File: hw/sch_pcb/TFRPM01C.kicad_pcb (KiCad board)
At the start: 2 copper layers, 37.5 x 19 mm, 22 parts, among them J1 HEADER_1x03, J2 SM04B-GHS-TB, J3 SM04B-GHS-TB, M2 M3, U1 PCF8583, U2 74HC1G14GW, U3 MIC5504-3.3YM5

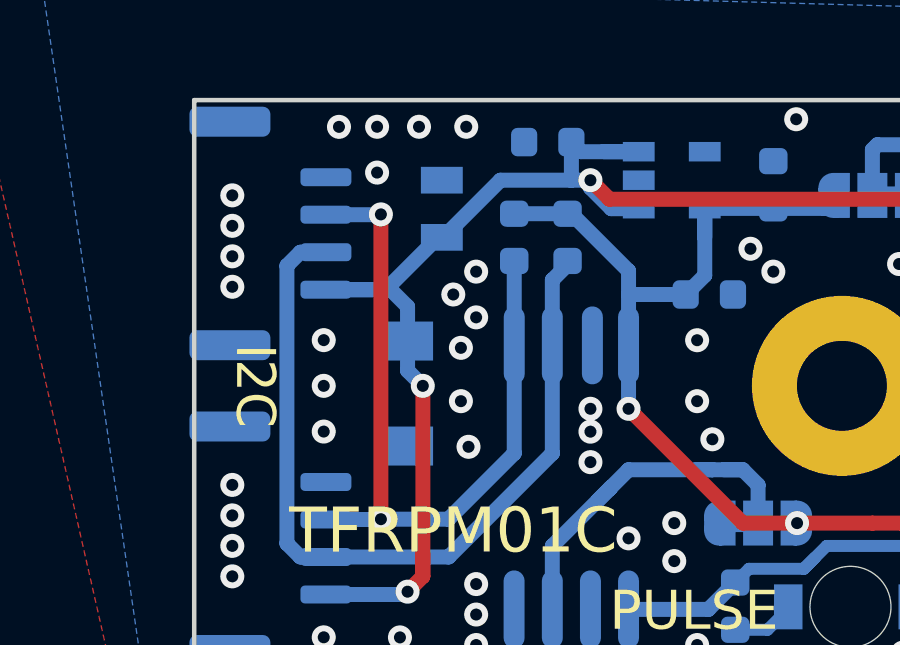
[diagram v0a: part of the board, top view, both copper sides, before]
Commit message: Edit labels PCB
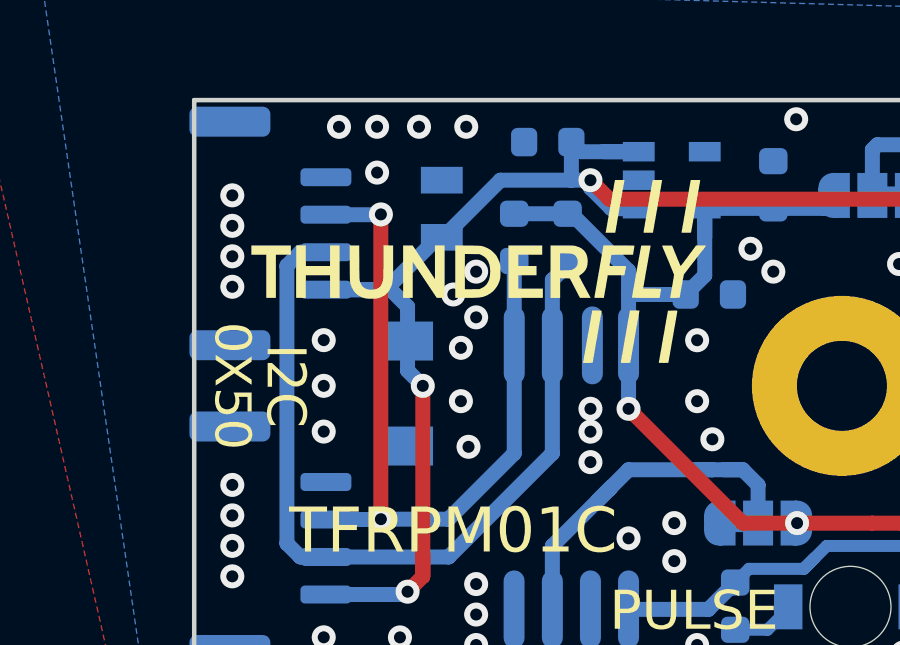
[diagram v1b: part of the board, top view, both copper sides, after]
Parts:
- added G***: LOGO, MLAB_LOGA:TF, F.Cu at (120.4, 128.5)
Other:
- board text added: "0X50"

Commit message: Edit PCB
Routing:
- net +5V: track 45.2 -> 45.8 mm
- net GND: vias 62 -> 63
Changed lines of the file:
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@@
   (via (at 119.888 131.064) (size 0.8) (drill 0.4) (layers "F.Cu" "B.Cu") (net 1))
   (via (at 120.396 139.954) (size 0.8) (drill 0.4) (layers "F.Cu" "B.Cu") (net 1))
+  (via (at 136.906 136.652) (size 0.8) (drill 0.4) (layers "F.Cu" "B.Cu") (net 1))
   (via (at 120.0658 123.695096) (size 0.8) (drill 0.4) (layers "F.Cu" "B.Cu") (net 1))
   (via (at 135.636 136.144) (size 0.8) (drill 0.4) (layers "F.Cu" "B.Cu") (net 1))
@@
   (segment (start 125.476 130.982) (end 125.476 133.096) (width 0.5) (layer "B.Cu") (net 4))
   (segment (start 139.05 140.142) (end 137.988 140.142) (width 0.5) (layer "B.Cu") (net 4))
+  (segment (start 118.618 139.446) (end 118.618 138.684) (width 0.5) (layer "F.Cu") (net 5))
   (segment (start 135.001 126.111) (end 124.841 126.111) (width 0.5) (layer "F.Cu") (net 5))
-  (segment (start 118.11 139.192) (end 118.618 138.684) (width 0.5) (layer "F.Cu") (net 5))
   (segment (start 118.618 138.684) (end 118.618 137.919096) (width 0.5) (layer "F.Cu") (net 5))
   (segment (start 124.841 126.111) (end 124.206 125.476) (width 0.5) (layer "F.Cu") (net 5))
   (segment (start 118.618 138.684) (end 118.618 132.331096) (width 0.5) (layer "F.Cu") (net 5))
   (via (at 118.618 132.331096) (size 0.8) (drill 0.4) (layers "F.Cu" "B.Cu") (net 5))
-  (via (at 118.11 139.192) (size 0.8) (drill 0.4) (layers "F.Cu" "B.Cu") (net 5))
+  (via (at 118.618 139.446) (size 0.8) (drill 0.4) (layers "F.Cu" "B.Cu") (net 5))
   (via (at 124.206 125.476) (size 0.8) (drill 0.4) (layers "F.Cu" "B.Cu") (net 5))
   (via (at 135.001 126.111) (size 0.8) (drill 0.4) (layers "F.Cu" "B.Cu") (net 5))
+  (segment (start 115.388 139.286096) (end 118.458096 139.286096) (width 0.5) (layer "B.Cu") (net 5))
   (segment (start 125.816 124.526) (end 124.648 124.526) (width 0.5) (layer "B.Cu") (net 5))
   (segment (start 124.206 125.476) (end 123.571 125.476) (width 0.5) (layer "B.Cu") (net 5))
@@
   (segment (start 121.20602 125.476) (end 119.30102 127.381) (width 0.5) (layer "B.Cu") (net 5))
   (segment (start 115.388 129.126096) (end 117.253904 129.126096) (width 0.5) (layer "B.Cu") (net 5))
-  (segment (start 115.388 139.286096) (end 118.015904 139.286096) (width 0.5) (layer "B.Cu") (net 5))
   (segment (start 118.11 130.838) (end 118.11 131.823096) (width 0.5) (layer "B.Cu") (net 5))
   (segment (start 125.816 124.526) (end 123.891 124.526) (width 0.5) (layer "B.Cu") (net 5))
   (segment (start 118.11 130.838) (end 118.11 129.688) (width 0.5) (layer "B.Cu") (net 5))
-  (segment (start 118.015904 139.286096) (end 118.11 139.192) (width 0.5) (layer "B.Cu") (net 5))
   (segment (start 117.380904 129.126096) (end 117.548096 128.958904) (width 0.5) (layer "B.Cu") (net 5))
+  (segment (start 118.458096 139.286096) (end 118.618 139.446) (width 0.5) (layer "B.Cu") (net 5))
   (segment (start 124.206 125.73) (end 124.206 125.476) (width 0.5) (layer "B.Cu") (net 5))
   (segment (start 123.571 125.476) (end 121.20602 125.476) (width 0.5) (layer "B.Cu") (net 5))
